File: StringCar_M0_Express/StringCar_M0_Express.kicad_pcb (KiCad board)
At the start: 2 copper layers, 50.8 x 22.9 mm, 47 parts, among them J1 USB_MICRO, J2 SENSOR_IN, J3 SWD, J4 STEMMA-QT, J5 MOTOR, J6 LIPO_BATT, Q1 DMG2305UX-13, Q2 DMG2305UX-13, SW1 RESET, SW2 POWER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

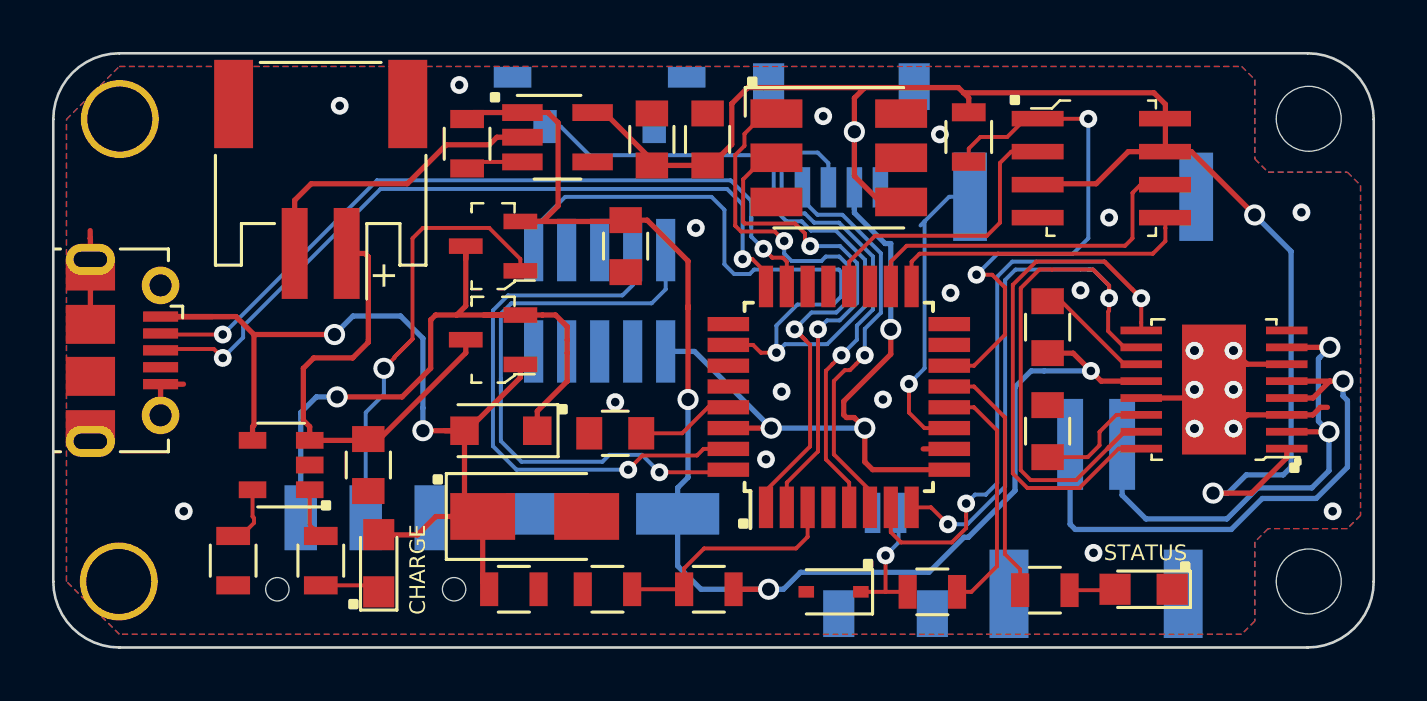
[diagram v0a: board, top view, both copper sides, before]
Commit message: repair schematic and regenerate PCB as v05
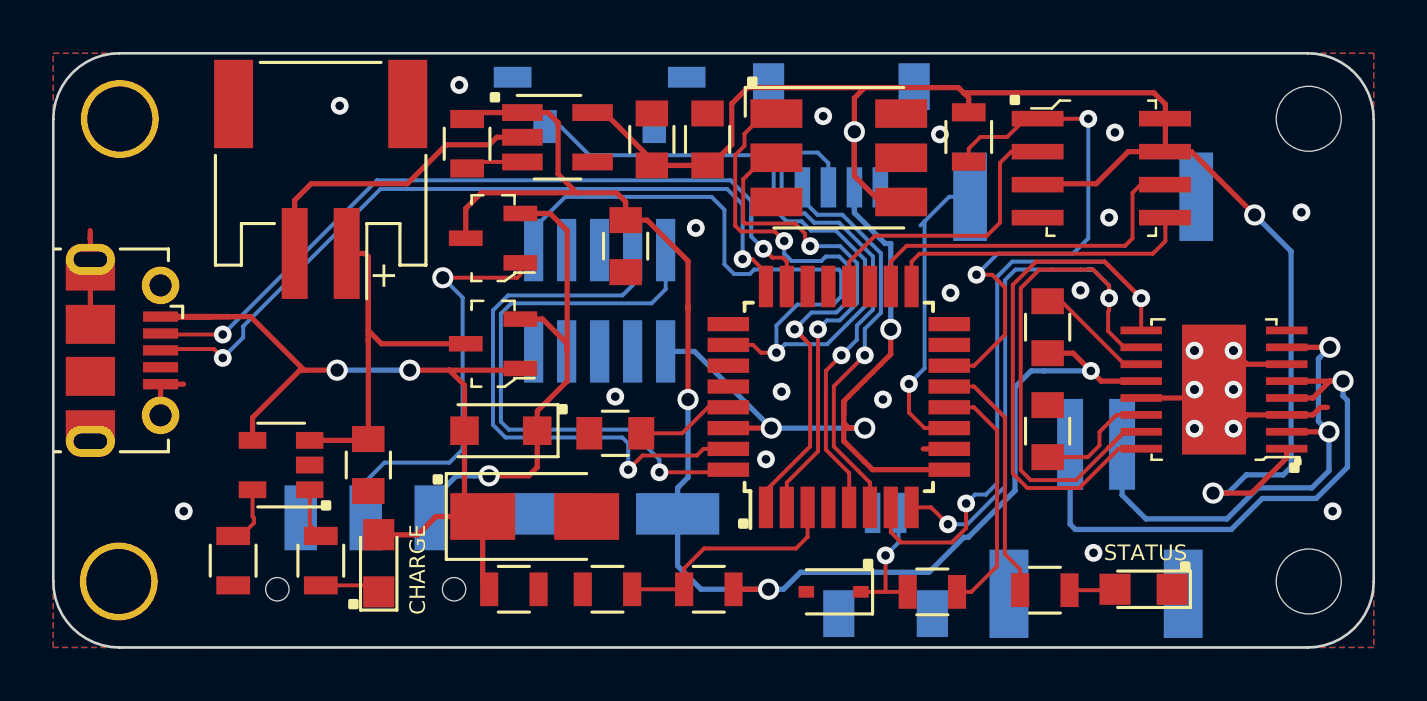
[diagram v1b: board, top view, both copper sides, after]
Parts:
- moved Q2 0.31 mm to (110.9, 101.1)
- moved Q1 0.16 mm to (110.9, 105.2)
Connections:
- Q2 pad 2: /V+ -> /Vbus
- Q2 pad 3: /Vbus -> /V+
- SW2 pad 1: GND -> /Vbus
- SW2 pad 3: /Vbus -> GND
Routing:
- net /Vbus: track 26.7 -> 19.4 mm
- net /V+: track 55.3 -> 57.7 mm
- net Net-(Q2-Pad1): track 17.6 -> 16.0 mm
- net +3V3: track 90.6 -> 91.8 mm
- net /VBUS: track 40.0 -> 39.2 mm
- net GND: vias 22 -> 23
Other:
- board text added: "2020-01-18 v05"
- board text removed: "2019-10-20 v04"

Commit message: correct stemma-qt pinout
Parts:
- added G***: LOGO, Adafruit:CG_logo_25-4mm, B.Cu at (104.4, 105.4)
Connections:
- J1 pad 4: (no net) -> Net-(J1-Pad4)
- J3 pad 6: (no net) -> Net-(J3-Pad6)
- J3 pad 8: (no net) -> Net-(J3-Pad8)
- J4 pad 1: /SCL -> GND
- J4 pad 2: /SDA -> +3V3
- J4 pad 3: +3V3 -> /SDA
- J4 pad 4: GND -> /SCL
- LED2 pad 5: (no net) -> Net-(LED2-Pad5)
- LED2 pad 6: (no net) -> Net-(LED2-Pad6)
- U1 pad 15: (no net) -> Net-(U1-Pad15)
- U1 pad 16: (no net) -> Net-(U1-Pad16)
- U1 pad 19: (no net) -> Net-(U1-Pad19)
- U1 pad 21: (no net) -> Net-(U1-Pad21)
- U1 pad 22: (no net) -> Net-(U1-Pad22)
- U1 pad 25: (no net) -> Net-(U1-Pad25)
- U1 pad 27: (no net) -> Net-(U1-Pad27)
- U1 pad 4: (no net) -> Net-(U1-Pad4)
- U3 pad 8: (no net) -> Net-(U3-Pad8)
- U5 pad 4: (no net) -> Net-(U5-Pad4)
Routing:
- net GND: track 27.0 -> 17.8 mm
- net /SDA: track 19.8 -> 13.7 mm
- net +3V3: track 91.8 -> 96.8 mm
- net /SCL: track 15.4 -> 14.2 mm
- net /V+: track 57.7 -> 58.4 mm
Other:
- board text added: "2020-07-31 v06"
- board text removed: "2020-01-18 v05"

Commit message: update PCB
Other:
- board text added: "2020-08-05 v06"
- board text added: "3V3 GND"
- board text added: "D C"
- board text added: "SCL SDA 3V GND"
- board text removed: "--GND--"
- board text removed: "2020-07-31 v06"
- board text removed: "3V"
- board text removed: "C"
- board text removed: "D"
- board text removed: "G 3V SDA SCL"
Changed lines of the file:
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@@
   (general
     (thickness 1.6)
-    (drawings 32)
+    (drawings 34)
     (tracks 581)
     (zones 0)
@@
   (title_block
     (title StringCar_M0_Express)
-    (date 2020-07-31)
+    (date 2020-08-05)
     (rev v06)
     (company "Cedar Grove Studios")
@@
     (visible_elements 7FFFFFFF)
     (pcbplotparams
-      (layerselection 0x010f8_ffffffff)
+      (layerselection 0x010fc_ffffffff)
       (usegerberextensions true)
       (usegerberattributes false)
@@
       (effects (font (size 0.4 0.4) (thickness 0.08)) (justify mirror))
     )
-    (fp_text value RESET (at 0 -1.7 180) (layer B.SilkS)
+    (fp_text value RESET (at 0 -1.89 180) (layer B.SilkS)
       (effects (font (size 0.6 0.6) (thickness 0.12)) (justify mirror))
     )
@@
       (xy -0.027237 1.36959) (xy 0.078018 1.358083)) (layer B.Mask) (width 0.01))
   )
+  (gr_line (start 112.141 107.696) (end 112.141 107.061) (layer B.SilkS) (width 0.15))
+  (gr_line (start 112.268 107.696) (end 112.141 107.696) (layer B.SilkS) (width 0.15))
+  (gr_line (start 116.332 107.696) (end 112.268 107.696) (layer B.SilkS) (width 0.15))
+  (gr_line (start 116.332 107.061) (end 116.332 107.696) (layer B.SilkS) (width 0.15))
   (gr_poly (pts (xy 137.4 113.6) (xy 137.654 113.6) (xy 137.654 113.854) (xy 137.4 113.854)) (layer F.SilkS) (width 0.15))
   (gr_poly (pts (xy 105.4 115.046) (xy 105.654 115.046) (xy 105.654 115.3) (xy 105.4 115.3)) (layer F.SilkS) (width 0.15))
@@
   (gr_poly (pts (xy 120.4 111.946) (xy 120.654 111.946) (xy 120.654 112.2) (xy 120.4 112.2)) (layer F.SilkS) (width 0.15))
   (gr_poly (pts (xy 130.846 95.646) (xy 131.1 95.646) (xy 131.1 95.9) (xy 130.846 95.9)) (layer F.SilkS) (width 0.15))
-  (gr_text --GND-- (at 116.7 107.3) (layer B.SilkS)
-    (effects (font (size 0.6 0.6) (thickness 0.12)) (justify left mirror))
-  )
-  (gr_text 3V (at 118.1 107.4) (layer B.SilkS)
-    (effects (font (size 0.6 0.6) (thickness 0.12)) (justify left mirror))
+  (gr_text "3V3    GND" (at 117.983 107.315) (layer B.SilkS)
+    (effects (font (size 0.5 0.5) (thickness 0.1)) (justify left mirror))
   )
   (gr_text CHARGE (at 108 112.1 90) (layer F.SilkS)
@@
     (effects (font (size 0.6 0.6) (thickness 0.12)))
   )
-  (gr_text D (at 117.9 99.7) (layer B.SilkS)
-    (effects (font (size 0.6 0.6) (thickness 0.12)) (justify left mirror))
+  (gr_text "D  C" (at 117.856 99.695) (layer B.SilkS)
+    (effects (font (size 0.5 0.5) (thickness 0.1)) (justify left mirror))
   )
   (gr_text ~R (at 112.8 99.7) (layer B.SilkS)
     (effects (font (size 0.6 0.6) (thickness 0.12)) (justify left mirror))
   )
-  (gr_text C (at 116.7 99.7) (layer B.SilkS)
-    (effects (font (size 0.6 0.6) (thickness 0.12)) (justify left mirror))
-  )
-  (gr_text "G 3V SDA SCL" (at 124.1 100.9) (layer B.SilkS)
-    (effects (font (size 0.6 0.6) (thickness 0.12)) (justify mirror))
+  (gr_text "SCL SDA 3V GND" (at 124.1 100.584) (layer B.SilkS)
+    (effects (font (size 0.5 0.5) (thickness 0.1)) (justify mirror))
   )
-  (gr_text "2020-07-31 v06" (at 117.2 115.9) (layer B.Mask)
+  (gr_text "2020-08-05 v06" (at 117.2 115.9) (layer B.Mask)
     (effects (font (size 0.5 0.5) (thickness 0.1)) (justify mirror))
   )
@@
   (via (at 118.7 100.7) (size 0.6858) (drill 0.3302) (layers F.Cu B.Cu) (net 1))
   (via (at 134.8232 97.028) (size 0.6858) (drill 0.3302) (layers F.Cu B.Cu) (net 1))
+  (segment (start 122.8 99.6125) (end 122.8 99.1375) (width 0.1524) (layer B.Cu) (net 1))
   (segment (start 126.6 99.7) (end 125.8 99.7) (width 0.2032) (layer F.Cu) (net 2))
   (segment (start 125.8 99.7) (end 124.8 98.7) (width 0.2032) (layer F.Cu) (net 2))
@@
   (segment (start 126.2 100.7) (end 127.4 99.5) (width 0.2032) (layer B.Cu) (net 2))
   (segment (start 126.2 104.6) (end 126.2 100.7) (width 0.2032) (layer B.Cu) (net 2))
+  (segment (start 123.8 99.1375) (end 123.8 97.4) (width 0.2032) (layer B.Cu) (net 2))
+  (segment (start 124.2 97) (end 124.8 97) (width 0.2032) (layer B.Cu) (net 2))
+  (segment (start 123.8 97.4) (end 124.2 97) (width 0.2032) (layer B.Cu) (net 2))
+  (segment (start 123.8 99.1375) (end 123.8 98.2) (width 0.2032) (layer B.Cu) (net 2))
   (segment (start 119.172078 107.6) (end 119.95 107.6) (width 0.1524) (layer F.Cu) (net 3))
   (segment (start 118.172078 108.6) (end 119.172078 107.6) (width 0.1524) (layer F.Cu) (net 3))
@@
   (segment (start 124.2 102.3) (end 120.945822 102.3) (width 0.1524) (layer B.Cu) (net 24))
   (segment (start 119.8 102.1) (end 119.8 100) (width 0.1524) (layer B.Cu) (net 24))
+  (segment (start 113.3 98.562801) (end 112.9 98.162801) (width 0.1524) (layer B.Cu) (net 24))
+  (segment (start 121.1372 99.536064) (end 120.163938 98.562802) (width 0.1524) (layer B.Cu) (net 24))
+  (segment (start 121.528499 100.628499) (end 121.1372 100.2372) (width 0.1524) (layer B.Cu) (net 24))
+  (segment (start 123.821697 100.628499) (end 121.528499 100.628499) (width 0.1524) (layer B.Cu) (net 24))
+  (segment (start 125.209369 102.016171) (end 123.821697 100.628499) (width 0.1524) (layer B.Cu) (net 24))
+  (segment (start 121.8 105.5) (end 122.128499 105.171501) (width 0.1524) (layer B.Cu) (net 24))
+  (segment (start 121.1372 100.2372) (end 121.1372 99.536064) (width 0.1524) (layer B.Cu) (net 24))
+  (segment (start 112.9 98.162801) (end 112.9 96.8) (width 0.1524) (layer B.Cu) (net 24))
+  (segment (start 125.20937 103.713512) (end 125.209369 102.016171) (width 0.1524) (layer B.Cu) (net 24))
+  (segment (start 123.751381 105.171501) (end 125.20937 103.713512) (width 0.1524) (layer B.Cu) (net 24))
+  (segment (start 120.163938 98.562802) (end 113.3 98.562801) (width 0.1524) (layer B.Cu) (net 24))
+  (segment (start 122.128499 105.171501) (end 123.751381 105.171501) (width 0.1524) (layer B.Cu) (net 24))
   (segment (start 118.4 107.3) (end 118.4 107.3) (width 0.2032) (layer F.Cu) (net 25))
   (via (at 118.4 107.3) (size 0.8128) (drill 0.508) (layers F.Cu B.Cu) (net 25))
@@
   (segment (start 118.4 101.9718) (end 118.4 103.8) (width 0.2032) (layer F.Cu) (net 25))
   (segment (start 116 100.4) (end 116.8282 100.4) (width 0.2032) (layer F.Cu) (net 25))
+  (segment (start 109.291358 99.35) (end 108.8 98.858642) (width 0.2032) (layer F.Cu) (net 25))
+  (segment (start 110.45 99.35) (end 109.291358 99.35) (width 0.2032) (layer F.Cu) (net 25))
+  (segment (start 108.8 97.1) (end 108.8 96.7) (width 0.2032) (layer F.Cu) (net 25))
+  (segment (start 108.8 98.858642) (end 108.8 97.1) (width 0.2032) (layer F.Cu) (net 25))
+  (segment (start 108.99 96.51) (end 109.9 96.51) (width 0.2032) (layer F.Cu) (net 25))
+  (segment (start 108.8 96.7) (end 108.99 96.51) (width 0.2032) (layer F.Cu) (net 25))
   (via (at 108.966 102.616) (size 0.8128) (drill 0.508) (layers F.Cu B.Cu) (net 26))
   (segment (start 109.728 103.378) (end 108.966 102.616) (width 0.1524) (layer B.Cu) (net 26))
@@
   (segment (start 127.5 100.4476) (end 127.5 106.099996) (width 0.1524) (layer B.Cu) (net 28))
   (via (at 125.2 105.6) (size 0.6858) (drill 0.3302) (layers F.Cu B.Cu) (net 29))
-  (segment (start 122.8 99.6125) (end 122.8 99.1375) (width 0.1524) (layer B.Cu) (net 1))
-  (segment (start 123.8 99.1375) (end 123.8 97.4) (width 0.2032) (layer B.Cu) (net 2))
-  (segment (start 124.2 97) (end 124.8 97) (width 0.2032) (layer B.Cu) (net 2))
-  (segment (start 123.8 97.4) (end 124.2 97) (width 0.2032) (layer B.Cu) (net 2))
-  (segment (start 123.8 99.1375) (end 123.8 98.2) (width 0.2032) (layer B.Cu) (net 2))
-  (segment (start 113.3 98.562801) (end 112.9 98.162801) (width 0.1524) (layer B.Cu) (net 24))
-  (segment (start 121.1372 99.536064) (end 120.163938 98.562802) (width 0.1524) (layer B.Cu) (net 24))
-  (segment (start 121.528499 100.628499) (end 121.1372 100.2372) (width 0.1524) (layer B.Cu) (net 24))
-  (segment (start 123.821697 100.628499) (end 121.528499 100.628499) (width 0.1524) (layer B.Cu) (net 24))
-  (segment (start 125.209369 102.016171) (end 123.821697 100.628499) (width 0.1524) (layer B.Cu) (net 24))
-  (segment (start 121.8 105.5) (end 122.128499 105.171501) (width 0.1524) (layer B.Cu) (net 24))
-  (segment (start 121.1372 100.2372) (end 121.1372 99.536064) (width 0.1524) (layer B.Cu) (net 24))
-  (segment (start 112.9 98.162801) (end 112.9 96.8) (width 0.1524) (layer B.Cu) (net 24))
-  (segment (start 125.20937 103.713512) (end 125.209369 102.016171) (width 0.1524) (layer B.Cu) (net 24))
-  (segment (start 123.751381 105.171501) (end 125.20937 103.713512) (width 0.1524) (layer B.Cu) (net 24))
-  (segment (start 120.163938 98.562802) (end 113.3 98.562801) (width 0.1524) (layer B.Cu) (net 24))
-  (segment (start 122.128499 105.171501) (end 123.751381 105.171501) (width 0.1524) (layer B.Cu) (net 24))
-  (segment (start 109.291358 99.35) (end 108.8 98.858642) (width 0.2032) (layer F.Cu) (net 25))
-  (segment (start 110.45 99.35) (end 109.291358 99.35) (width 0.2032) (layer F.Cu) (net 25))
-  (segment (start 108.8 97.1) (end 108.8 96.7) (width 0.2032) (layer F.Cu) (net 25))
-  (segment (start 108.8 98.858642) (end 108.8 97.1) (width 0.2032) (layer F.Cu) (net 25))
-  (segment (start 108.99 96.51) (end 109.9 96.51) (width 0.2032) (layer F.Cu) (net 25))
-  (segment (start 108.8 96.7) (end 108.99 96.51) (width 0.2032) (layer F.Cu) (net 25))
   (segment (start 124.00962 106.79038) (end 125.2 105.6) (width 0.1524) (layer F.Cu) (net 29))
   (segment (start 124.00962 109.10722) (end 124.00962 106.79038) (width 0.1524) (layer F.Cu) (net 29))
